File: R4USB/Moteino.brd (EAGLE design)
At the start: 44.7 x 23.1 mm, 29 parts, among them CN1 MINIB, IC1 FT232RL, IC3 MCP1703CB, X1 16 MHz

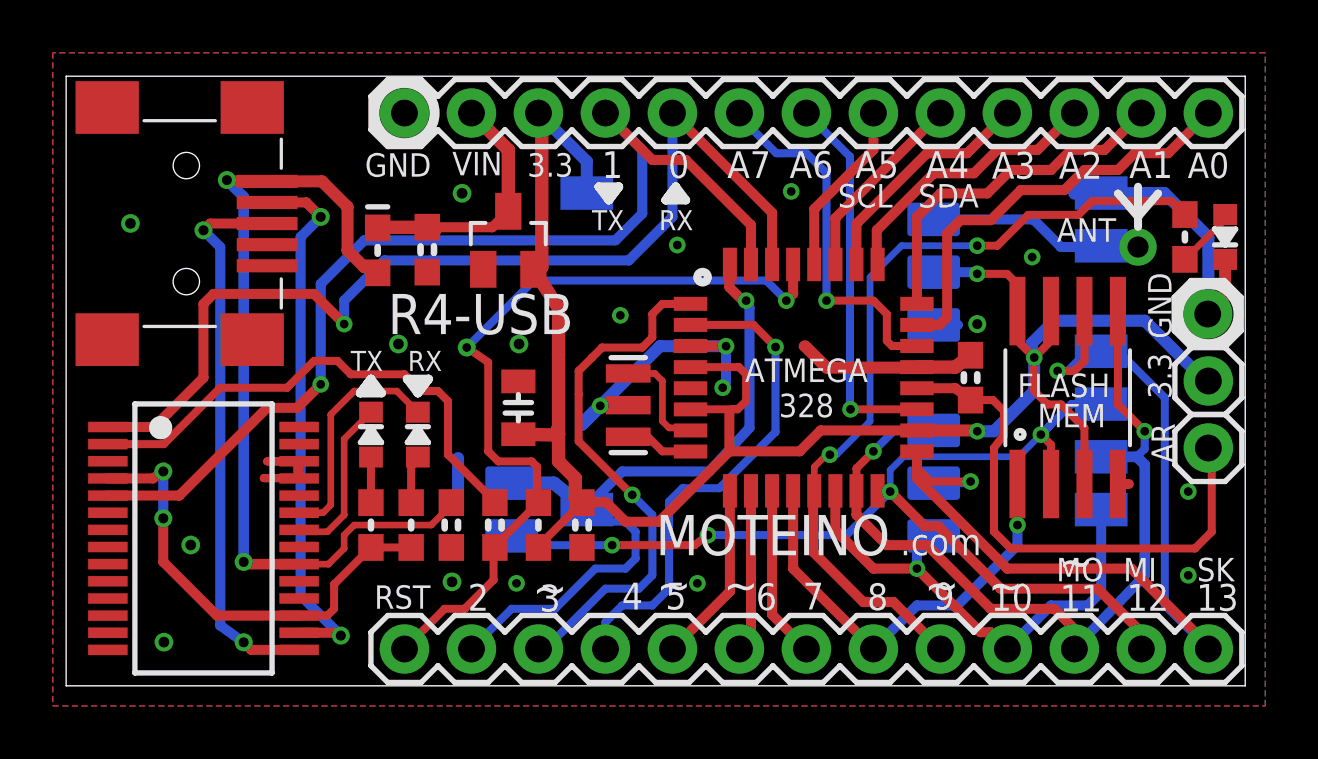
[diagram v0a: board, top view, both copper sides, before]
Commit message: Update Eagle files, add schematic PDFs
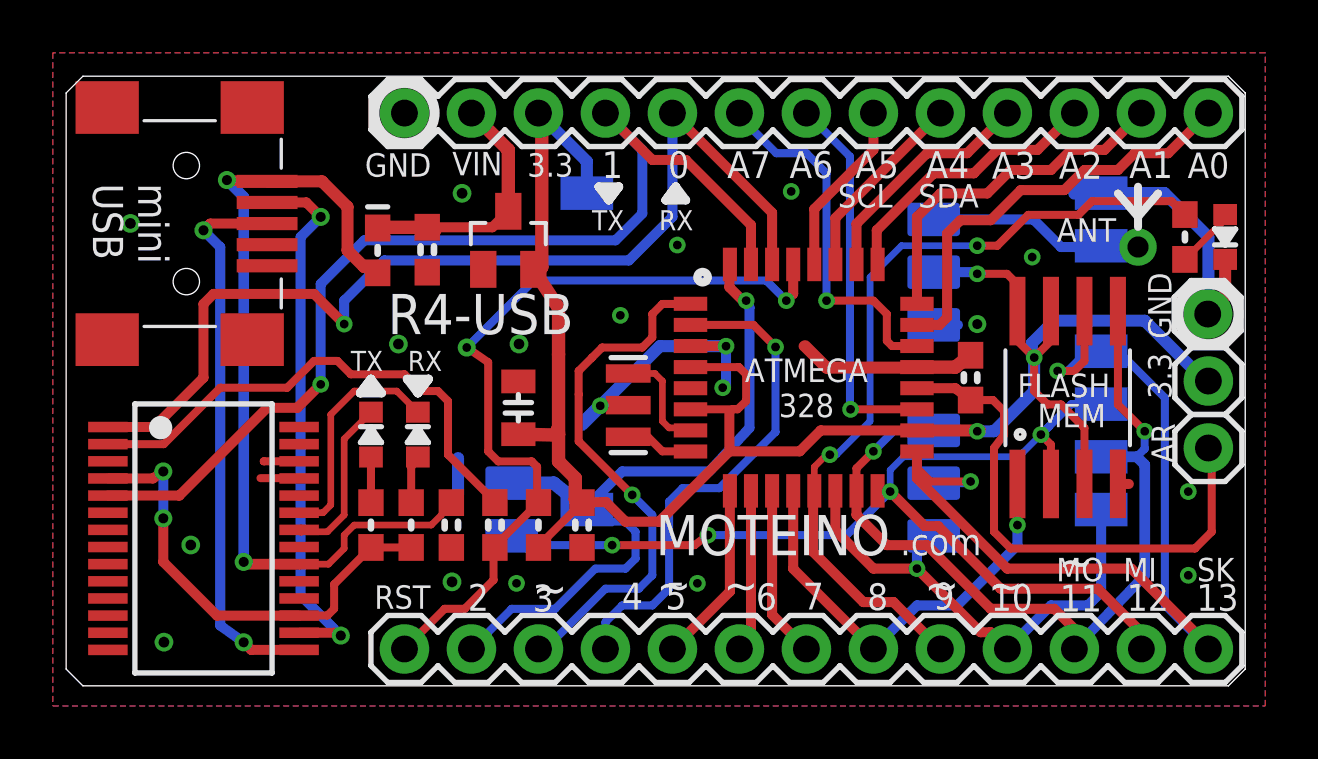
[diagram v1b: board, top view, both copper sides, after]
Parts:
- moved U$3 0.13 mm to (15.4, 11.3)
- renumbered U$6 to W25X40CLSNIG-ND
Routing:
- net GND: track 41.9 -> 38.0 mm
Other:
- outline, holes or cut-outs redrawn
- board text added: "434"
- board text added: "868"
- board text added: "915"
- board text added: "For use with: RFM12B / RFM69"
- board text added: "USB Powered"
- board text added: "XXXXXXXXXXXX"
- board text added: "mini USB"
- board text removed: "USB Powered or VIN: 3.3-12V"
